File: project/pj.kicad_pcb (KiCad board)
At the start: 2 copper layers, 65 x 56.5 mm, 17 parts, among them J1 RPi_GPIO, J10 PWR enable, J2 2B+, J3 zero, J4 3A+, J5 3B+, J6 4, J7 Conn_01x02, J8 Conn_01x02, J9 External PWR, SW1 SW_Push, SW2 SW_Push

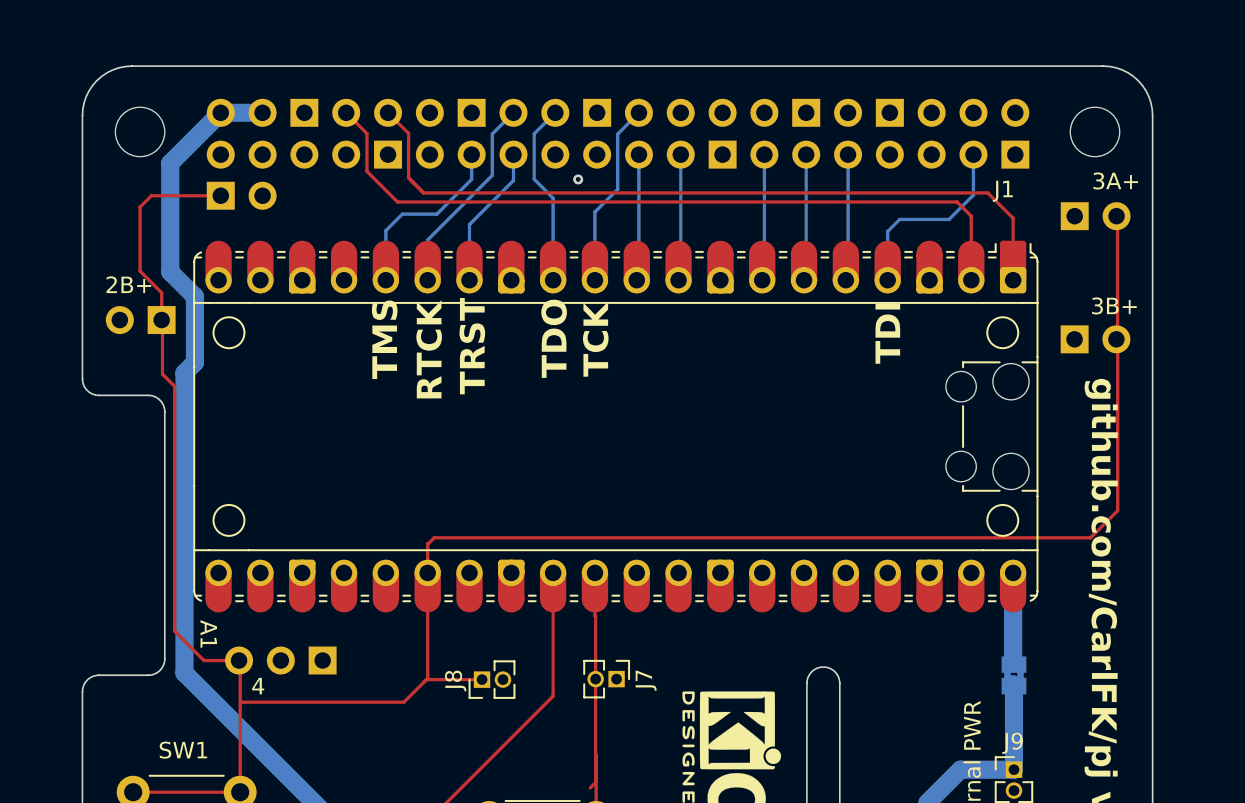
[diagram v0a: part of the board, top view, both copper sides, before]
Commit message: added 40 pin socket
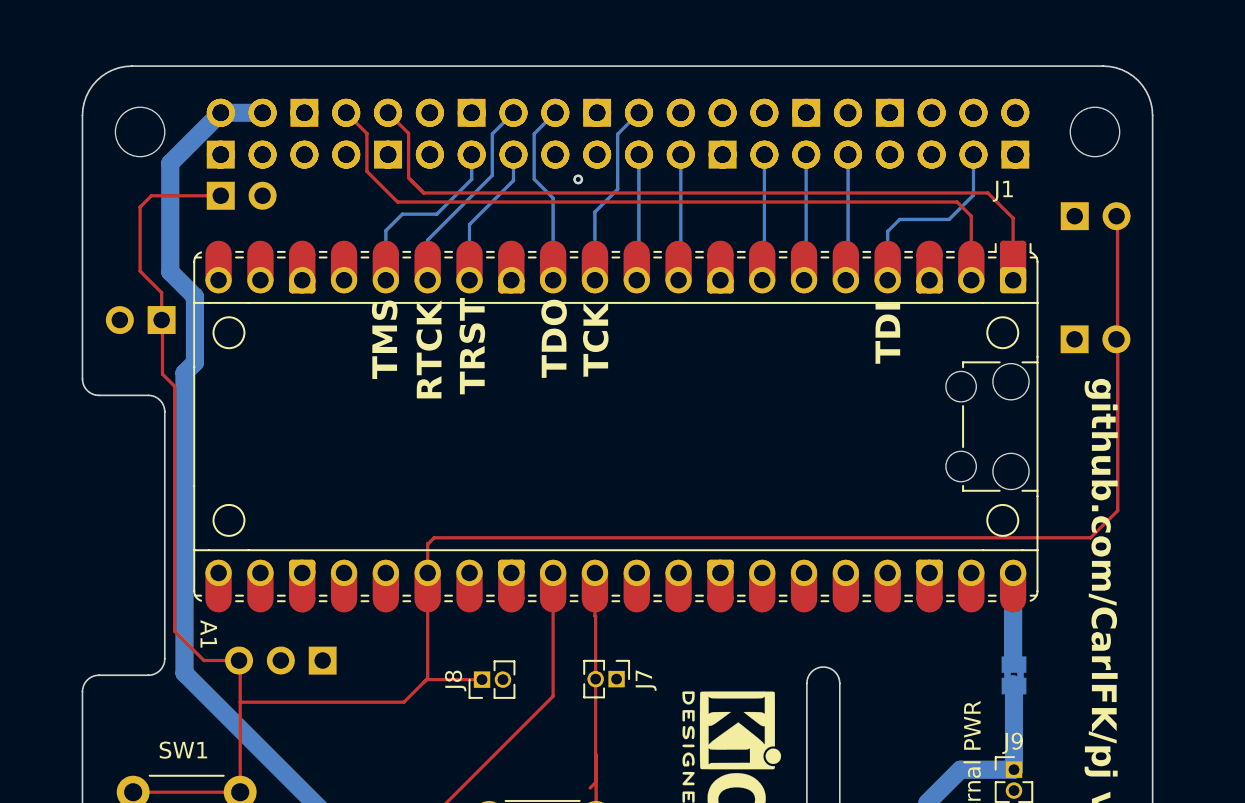
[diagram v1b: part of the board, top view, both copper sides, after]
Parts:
- added REF**: PinSocket_2x20_P2.54mm_Vertical, Connector_PinSocket_2.54mm:PinSocket_2x20_P2.54mm_Vertical, B.Cu at (44.8, 45.9)
- J2, J3, J4, J5: footprint Connector_PinHeader_2.54mm:PinHeader_1x02_P2.54mm_Vertical -> Connector_PinSocket_2.54mm:PinSocket_1x02_P2.54mm_Vertical
- J6: footprint Connector_PinHeader_2.54mm:PinHeader_1x03_P2.54mm_Vertical -> Connector_PinSocket_2.54mm:PinSocket_1x03_P2.54mm_Vertical

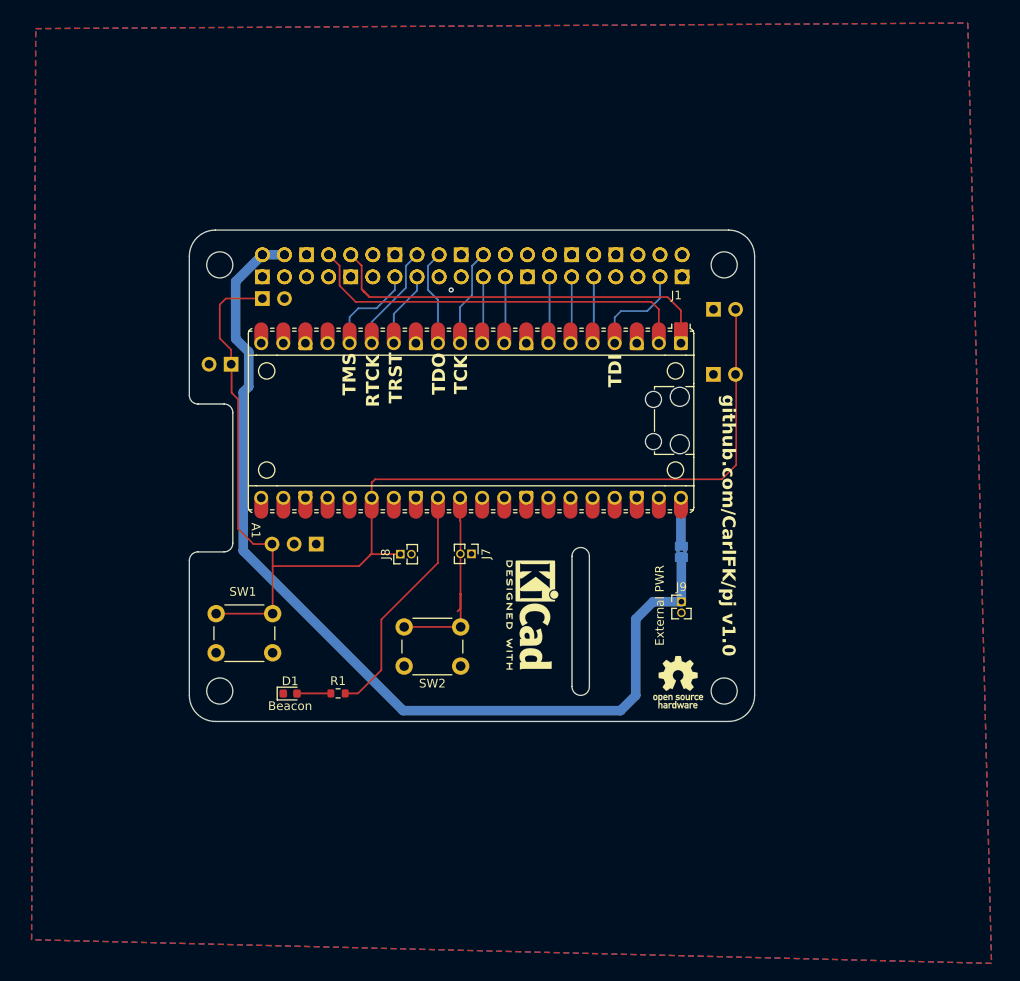
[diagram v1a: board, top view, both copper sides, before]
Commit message: group jtag io
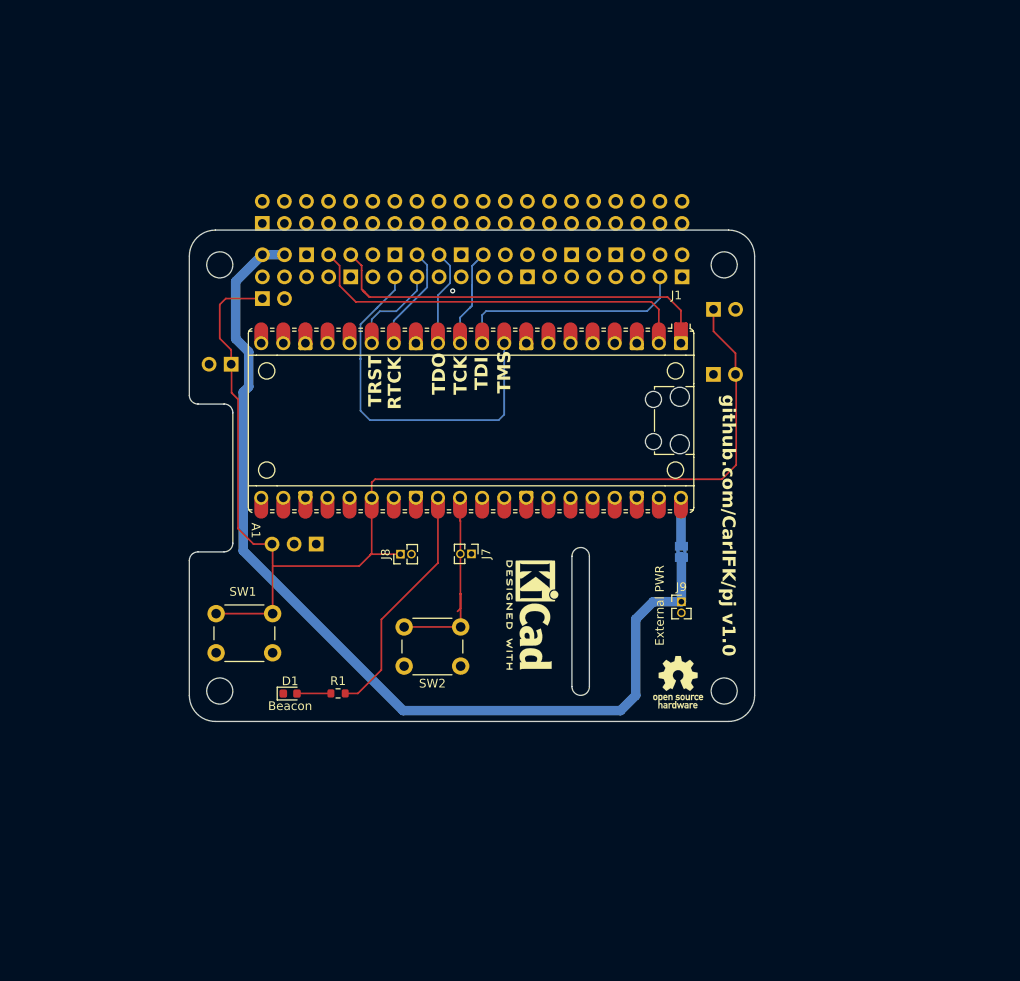
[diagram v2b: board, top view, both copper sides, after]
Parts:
- J10: value PWR enable -> Pico PWR enable
- J2, J3, J4, J5: footprint Connector_PinSocket_2.54mm:PinSocket_1x02_P2.54mm_Vertical -> Connector_PinHeader_2.54mm:PinHeader_1x02_P2.54mm_Vertical
- J6: footprint Connector_PinSocket_2.54mm:PinSocket_1x03_P2.54mm_Vertical -> Connector_PinHeader_2.54mm:PinHeader_1x03_P2.54mm_Vertical
- moved REF** 6.14 mm to (44.8, 39.7)
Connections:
- net Net-(A1-GPIO8) renamed /TCK
- net Net-(A1-GPIO9) renamed /TDO
- A1 pad 10: /b5 -> /TDI
- A1 pad 14: Net-(A1-GPIO10) -> /RTCK
- A1 pad 15: Net-(A1-GPIO11) -> /TRST
- A1 pad 16: Net-(A1-GPIO12) -> unconnected-(A1-GPIO12-Pad16)
- A1 pad 4: Net-(A1-GPIO2) -> unconnected-(A1-GPIO2-Pad4)
- A1 pad 5: /b1 -> unconnected-(A1-GPIO3-Pad5)
- A1 pad 6: /b2 -> unconnected-(A1-GPIO4-Pad6)
- A1 pad 7: /b3 -> unconnected-(A1-GPIO5-Pad7)
- A1 pad 9: /b4 -> /TMS
- J1 pad 13: Net-(A1-GPIO12) -> /TMS
- J1 pad 15: Net-(A1-GPIO10) -> /TRST
- J1 pad 16: Net-(A1-GPIO11) -> /RTCK
- J1 pad 21: /b5 -> unconnected-(J1-BCM9_MISO-Pad21)
- J1 pad 23: /b4 -> unconnected-(J1-BCM11_SCLK-Pad23)
- J1 pad 27: /b3 -> unconnected-(J1-BCM0_ID_SD-Pad27)
- J1 pad 29: /b2 -> unconnected-(J1-BCM5-Pad29)
- J1 pad 31: /b1 -> unconnected-(J1-BCM6-Pad31)
- J1 pad 37: Net-(A1-GPIO2) -> /TDI
- J4 pad 1: unconnected-(J4-Pin_1-Pad1) -> Net-(A1-GPIO20)
- J4 pad 2: Net-(A1-GPIO20) -> unconnected-(J4-Pin_2-Pad2)
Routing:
- net /TMS: track 0.00 -> 42.9 mm
- net /TDI: track 0.00 -> 27.1 mm
- net Net-(A1-GPIO11): track 12.3 -> 0.00 mm
- net /RTCK: track 0.00 -> 12.2 mm
- net Net-(A1-GPIO2): track 11.5 -> 0.00 mm
- net Net-(A1-GPIO12): track 11.0 -> 0.00 mm
- net /TRST: track 0.00 -> 10.9 mm
- net Net-(A1-GPIO10): track 8.73 -> 0.00 mm
- net /b4: track 7.68 -> 0.00 mm
- net /b3: track 7.68 -> 0.00 mm
- net /b1: track 7.68 -> 0.00 mm
- net /b5: track 7.68 -> 0.00 mm
- net /b2: track 7.68 -> 0.00 mm
- net /TCK: track 11.4 -> 12.8 mm
- net Net-(A1-GPIO20): track 135.3 -> 136.3 mm
- removed copper zone on B.Cu, net GND
- removed copper zone on F.Cu, net GND

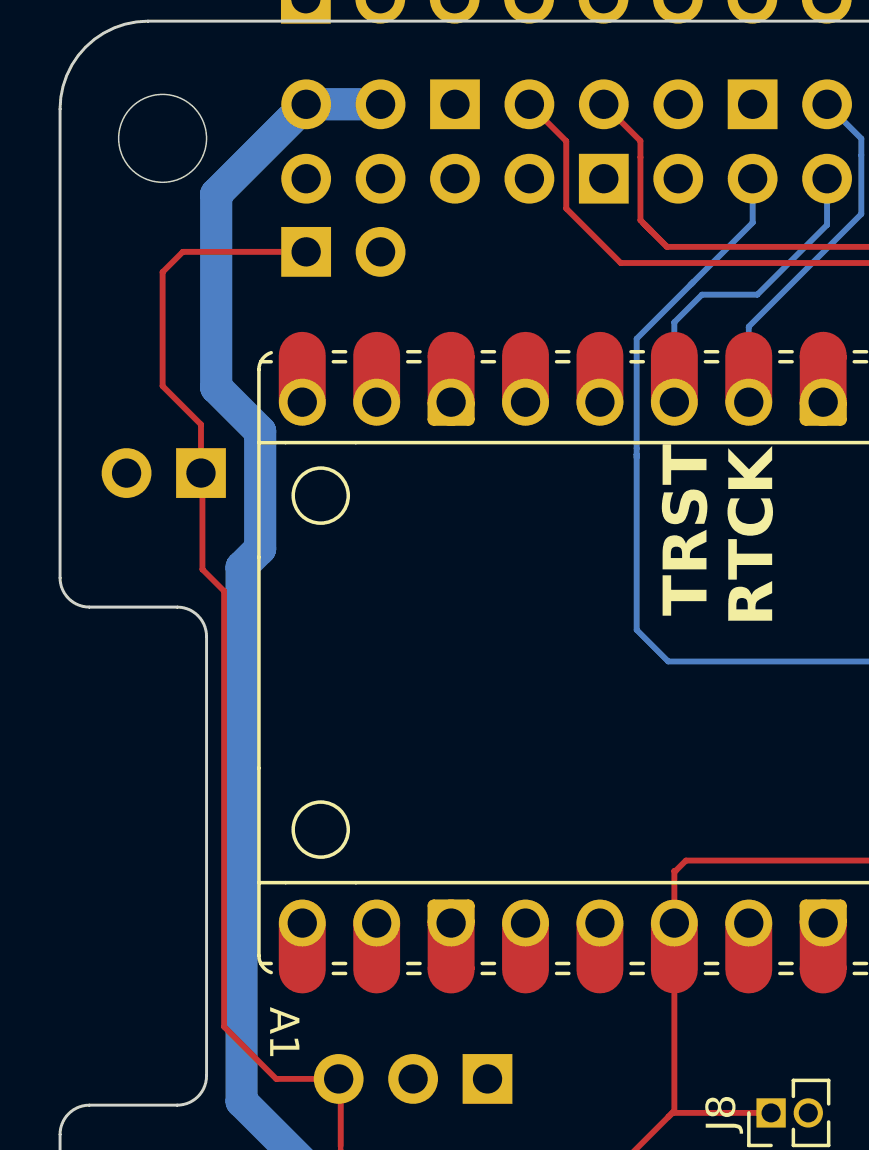
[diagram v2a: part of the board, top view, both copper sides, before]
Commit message: hook some gpios for kicks
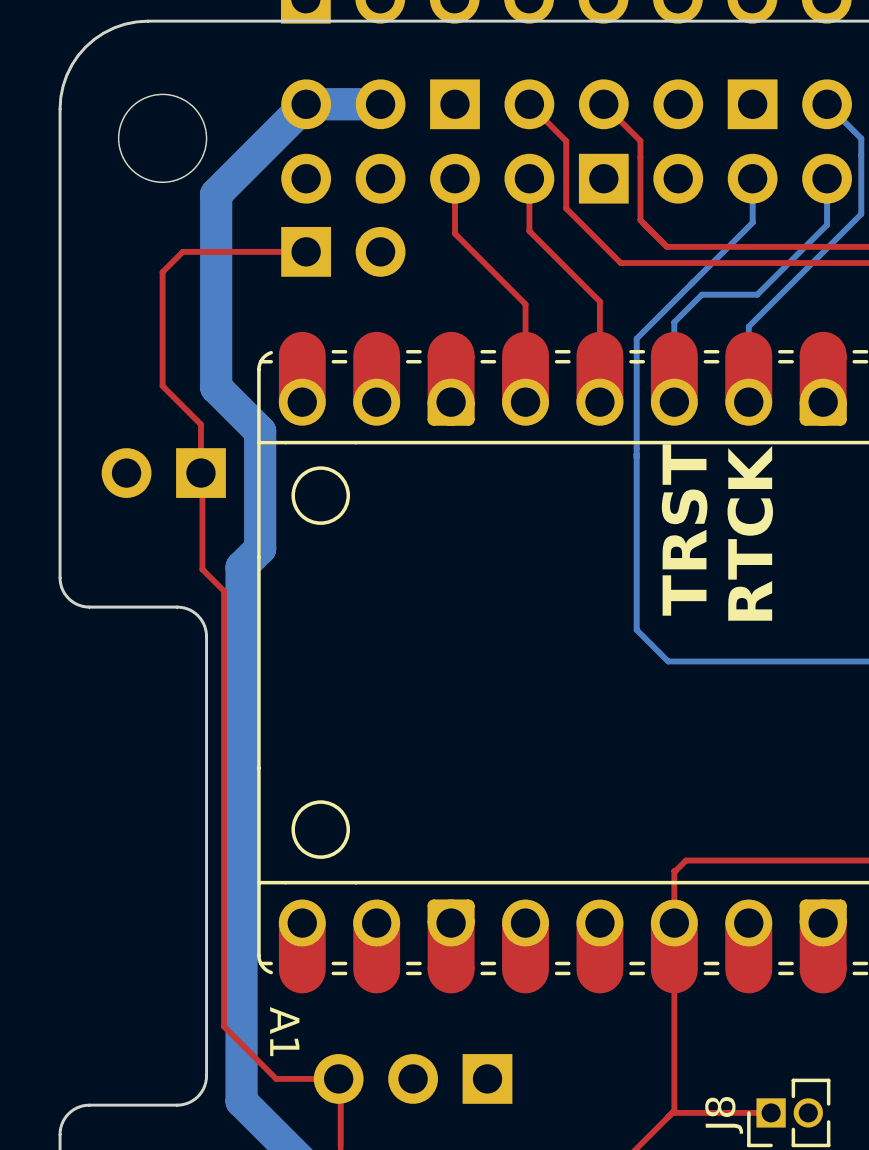
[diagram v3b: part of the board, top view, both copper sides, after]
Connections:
- A1 pad 16: unconnected-(A1-GPIO12-Pad16) -> Net-(A1-GPIO12)
- A1 pad 17: unconnected-(A1-GPIO13-Pad17) -> Net-(A1-GPIO13)
- J1 pad 5: unconnected-(J1-BCM3_SCL-Pad5) -> Net-(A1-GPIO13)
- J1 pad 7: unconnected-(J1-BCM4_GPCLK0-Pad7) -> Net-(A1-GPIO12)
- J4 pad 1: Net-(A1-GPIO20) -> unconnected-(J4-Pin_1-Pad1)
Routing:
- net Net-(A1-GPIO13): track 0.00 -> 8.62 mm
- net Net-(A1-GPIO12): track 0.00 -> 8.62 mm
